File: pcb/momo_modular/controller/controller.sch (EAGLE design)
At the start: 52 parts, among them Q1 MOSFET-N, Q2 P-MOSFET, U1 VOLTAGE-SUPERVISOR-BD45312, U2 PIC24FJ64GA306, U3 MCP1702, U4 RN4020_BT_4.0_MODULE, U5 FLASH8MSOP8, U6 MCP73811, U7 TS1102-CURRENT-SENSE

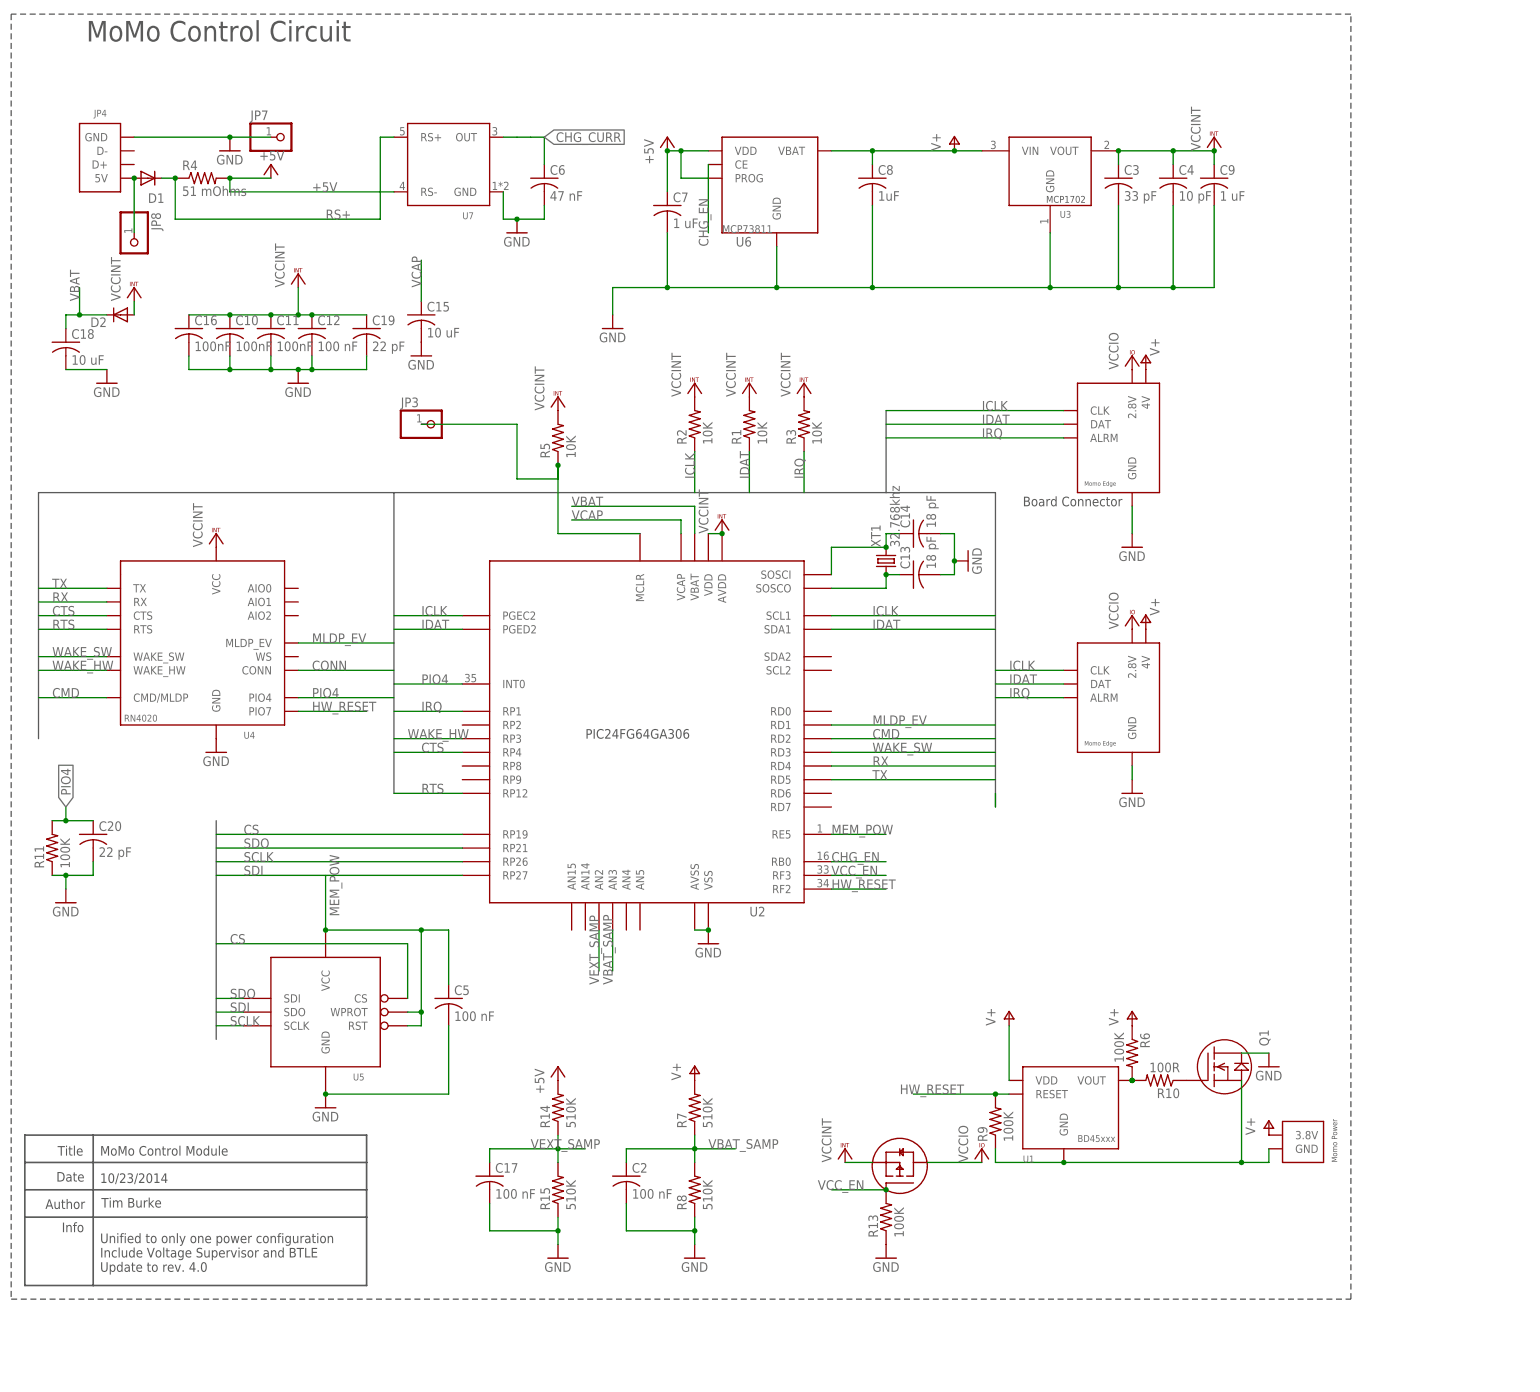
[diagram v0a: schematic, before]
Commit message: Merge pull request #141 from timburke/pr-controller-v4
Update Controller Hardware to Version 4.0

Update controller board to rev 4.0.

- New version contains BTLE via Microchip RN4020 module
- Voltage supervisor with hard reset capability from bluetooth
or via microcontroller
- Current monitor for solar and external charging current
- Move 2.8V linear regulator and add RF filtering caps to fix RF
interference problems on GSM transmission.

Merge pull request #141 from timburke/pr-controller-v4

Update Controller Hardware to Version 4.0

Update controller board to rev 4.0.

- New version contains BTLE via Microchip RN4020 module
- Voltage supervisor with hard reset capability from bluetooth
or via microcontroller
- Current monitor for solar and external charging current
- Move 2.8V linear regulator and add RF filtering caps to fix RF
interference problems on GSM transmission.

Rename combined_controller to controller

We don't have different assembly variants anymore so the
combined isn't needed.

Update controller board to version 4.1

- Fix parasitic path through hw reset controller by passing control
signal through an optocoupler
- Replace Li-ion battery charger IC with constant current regulator
to allow for solar panel charging
- Add solar panel current measurement with 1 ohm shunt and differential
ADC lines

Fix battery charging and simplify reset circuit.

- Remove MOSFET from battery- to minimize R on GSM power supply
- Add constant current charger for charging from external source
- Update parts to compatible versions with lower cost D1-3, Q2,4

Update part sizing document.

Update HW Reset components for increased reliability based on SPICE

- larger RC network on discharge FET.
- increased required assert time to 120 ms.
- reset pulse length: ~100 ms @ 25C

Rename controller board from combined_controller

Update controller project file.

Remove autorouter file.

Update labeling on schematic

Add spice models for controller battery charging and hw reset

U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
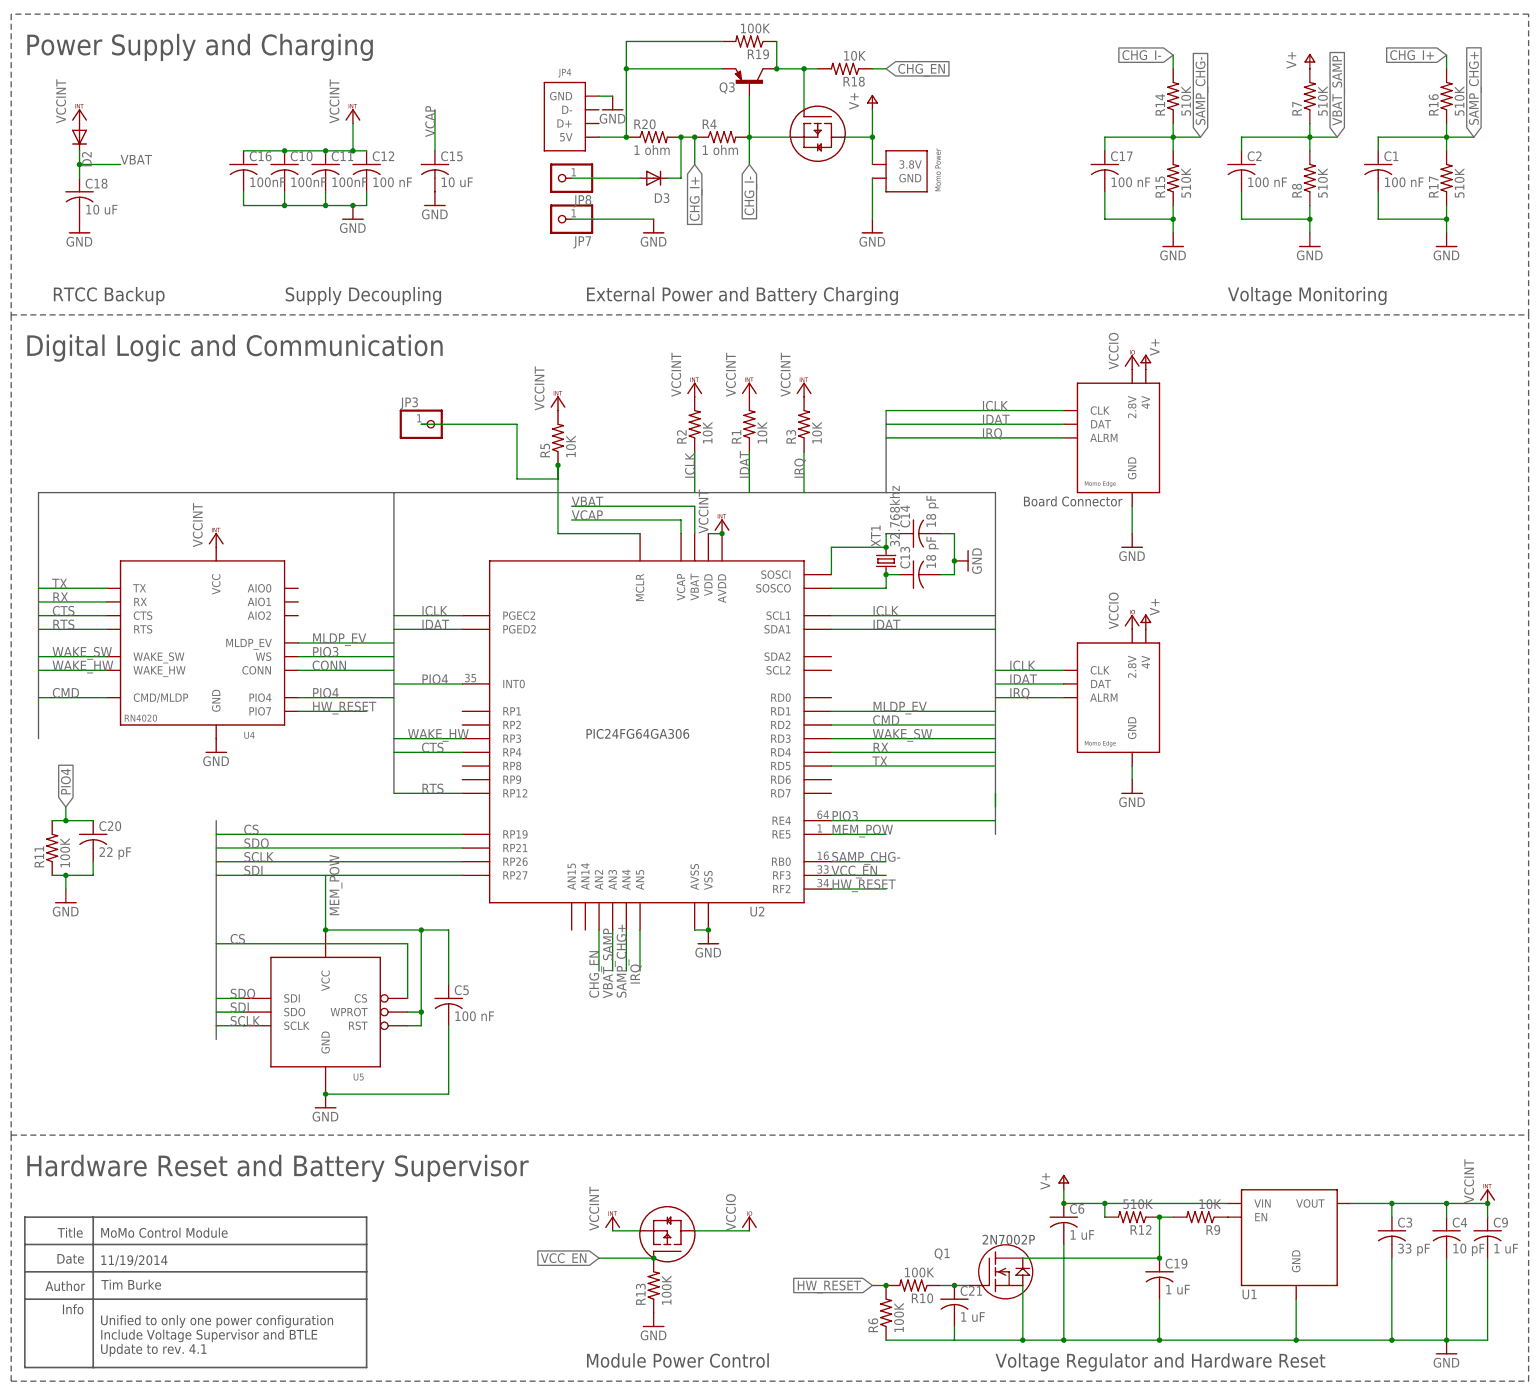
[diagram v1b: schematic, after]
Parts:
- removed C7: 1 uF, rcl:C-USC0402K
- removed C8: 1uF, rcl:C-USC0402K
- removed D1: (no value), diode:DIODE-SC79_INFINEON
- removed U3: MCP1702, components:MCP1702
- removed U6: MCP73811, components:MCP73811
- removed U7: TS1102-CURRENT-SENSE, custom_ics:TS1102-CURRENT-SENSE
- added C1: 100 nF, rcl:C-USC0402K
- added C21: 1 uF, rcl:C-USC0402K
- added D3: (no value), diode:DIODE-SC79_INFINEON
- added Q3: MMBTA56-SOT23, transistor-pnp:MMBTA56-SOT23
- added Q4: P-MOSFET, components:P-MOSFET
- added R12, R16, R17: 510K, rcl:R-US_R0603
- added R18: 10K, rcl:R-US_R0603
- added R19: 100K, rcl:R-US_R0603
- added R20: 1 ohm, rcl:R-US_R1206
- C19: value 22 pF -> 1 uF; DIGIKEY-PN 1276-1116-1-ND -> 445-4114-1-ND
- C6: value 47 nF -> 1 uF; DIGIKEY-PN 1276-1573-1-ND -> 445-4114-1-ND
- Q1: DESCRIPTION (none) -> N-Channel MOSFET 2N7002P; DIGIKEY-PN (none) -> 568-5818-1-ND
- Q2: DIGIKEY-PN (none) -> IRLML6402PBFCT-ND
- R10: value 100R -> 100K; DIGIKEY-PN RHM100CFCT-ND -> P100KHCT-ND
- R4: value 51 mOhms -> 1 ohm; device rcl:R-US_R0805 -> rcl:R-US_R1206; DIGIKEY-PN RHM.051NCT-ND -> 311-1.00FRCT-ND
- R9: value 100K -> 10K; DIGIKEY-PN P100KHCT-ND -> P10.0KHCT-ND
- U1: value VOLTAGE-SUPERVISOR-BD45312 -> XC6504-LINEAR-REGULATOR; device custom_ics:VOLTAGE-SUPERVISOR-BD45312 -> custom_ics:XC6504-LINEAR-REGULATOR
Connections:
- removed net +5V: C7.1, R14.2, R4.2, U6.PROG, U6.VDD, U7.RS-
- removed net CHG_CURR: C6.1, U7.OUT
- removed net N$8: R10.2, R6.2, U1.VOUT
- removed net N$9: D1.A, JP4.5V, JP8.1
- removed net RS+: D1.C, R4.1, U7.RS+
- removed net VEXT_SAMP: C17.1, R14.1, R15.2, U2.AN2
- new net CHG_I+: D3.C, R16.2, R20.2, R4.1
- new net CHG_I-: Q3.B, Q4.SOURCE, R14.2, R4.2
- new net N$10: Q3.C, Q4.GATE, R18.2, R19.1
- new net N$11: C19.1, Q1.D, R12.1, R9.2
- new net N$2: C21.1, Q1.G, R10.1
- new net N$3: D3.A, JP8.1
- new net PIO3: U2.RE4, U4.WS
- new net SAMP_CHG+: C1.1, R16.1, R17.2, U2.AN4
- new net SAMP_CHG-: C17.1, R14.1, R15.2, U2.RB0
- net CHG_EN: now also R18.1, U2.AN2; no longer U2.RB0, U6.CE
- net GND: now also C1.2, C21.2, JP5.GND, Q1.S, R17.1, R6.1, U1.GND; no longer C7.2, C8.2, Q1.D, U3.GND, U6.GND, U7.GND
- net HW_RESET: now also R10.2, R6.2; no longer R9.2, U1.RESET
- net IRQ: now also U2.AN5; no longer U2.RP1
- net N$1: now also R9.1, U1.EN; no longer Q1.G, R10.1
- net N$5: now also JP4.5V, Q3.E, R19.2, R20.1; no longer JP5.GND, Q1.S, R9.1, U1.GND
- net V+: now also C6.1, Q4.DRAIN, R12.2, U1.VIN; no longer C8.1, R6.1, U1.VDD, U3.VIN, U6.VBAT
- net VCCINT: now also U1.VOUT; no longer C19.1, U3.VOUT
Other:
- note added: "11/19/2014"
- note added: "2N7002P"
- note added: "Digital Logic and Communication"
- note added: "External Power and Battery Charging"
- note added: "Hardware Reset and Battery Supervisor"
- note added: "Module Power Control"
- note added: "Power Supply and Charging"
- note added: "RTCC Backup"
- note added: "Supply Decoupling"
- note added: "Unified to only one power configuration Include Voltage Supervisor and BTLE Update to rev. 4.1"
- note added: "Voltage Monitoring"
- note added: "Voltage Regulator and Hardware Reset"
- note removed: "10/23/2014"
- note removed: "MoMo Control Circuit"
- note removed: "Unified to only one power configuration Include Voltage Supervisor and BTLE Update to rev. 4.0"
- moved on the sheet: C10, C11, C12, C15, C16, C17, C18, C19, C2, C3, C4, C6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

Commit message: Update controller to v4.2
- Try to fix RF feedback issue using ferrite beads
- Add 100 uF tantalum output cap for better load stability
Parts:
- removed C18: 10 uF, rcl:C-USC0805K
- removed C19, C21: 1 uF, rcl:C-USC0402K
- removed C20: 22 pF, rcl:C-USC0402K
- removed C4: 10 pF, rcl:C-USC0402K
- removed D2: (no value), diode:DIODE-SC79_INFINEON
- removed Q1: MOSFET-N, custom_ics:MOSFET-N
- removed R10, R11, R6: 100K, rcl:R-US_R0603
- removed R12: 510K, rcl:R-US_R0603
- removed R9: 10K, rcl:R-US_R0603
- added FB1, FB2: (no value), rcl:R-US_R0603
- C3: value 33 pF -> 100 uF; device rcl:C-USC0402K -> rcl:CPOL-USB/3528-21R; DIGIKEY-PN 1276-1272-1-ND -> 478-8156-1-ND; FOOTPRINT (none) -> SMD1411
- U4: DIGIKEY-PN (none) -> RN4020-V/RM120-ND
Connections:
- removed net HW_RESET: R10.2, R6.2, U2.RF2, U4.PIO7
- removed net N$11: C19.1, Q1.D, R12.1, R9.2
- removed net PIO4: C20.1, R11.2, U2.INT0, U4.PIO4
- removed net VBAT: C18.1, D2.C, U2.VBAT
- net CONN: now also U2.INT0
- net GND: now also C3.-; no longer C18.2, C19.2, C20.2, C21.2, C3.2, C4.2, Q1.S, R11.1, R6.1
- net N$1: now also C3.+, C9.1, FB2.1, U1.VOUT; no longer R9.1, U1.EN
- net N$2: now also C6.1, FB1.2, U1.EN, U1.VIN; no longer C21.1, Q1.G, R10.1
- net V+: now also FB1.1; no longer C6.1, R12.2, U1.VIN
- net VCCINT: now also FB2.2, U2.VBAT; no longer C3.1, C4.1, C9.1, D2.A, U1.VOUT
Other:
- note removed: "2N7002P"
- moved on the sheet: C6, C9
